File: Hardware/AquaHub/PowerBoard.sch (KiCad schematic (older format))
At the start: 22 parts, among them J1 Screw_Terminal_01x02, J11 Power_Conn, J2 Screw_Terminal_01x02, J3 Screw_Terminal_01x02, J4 Screw_Terminal_01x02, J5 Screw_Terminal_01x02, J6 Screw_Terminal_01x02, J7 Control_Conn, J8 Screw_Terminal_01x02, K1 5A Relay, K2 5A Relay, K3 5A Relay, K4 5A Relay, K5 5A Relay, K6 5A Relay, U2 Current Sense

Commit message: Commit latest hardware updates and initial firmware
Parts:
- C1: Farnell (none) -> CA07658; manf# GRM033R61C104ME14D -> (none)
- C2: Mouser (none) -> VJ0603A102GXAPW1BC; manf# VJ0603A102GXAPW1BC -> x
- J1, J2, J3, J4, J5, J6: Mouser (none) -> 1935161; manf# 1935161 -> x
- J7: renamed from J8; Mouser (none) -> 1935161; manf# 1935161 -> x
- K1, K2, K3, K4, K5, K6: Mouser (none) -> FTR-F1AA012V; manf# FTR-F1AA012V -> x
- R1: Mouser (none) -> GWCR0603-10KFT5; manf# GWCR0603-10KFT5 -> (none)
- RV1: Mouser (none) -> B72214P2251K101; manf# B72214P2251K101 -> x
- U2: Mouser (none) -> MLX91210KDC-CAS-102-SP; manf# MLX91210KDC-CAS-102-SP -> x
- V1: Mouser (none) -> RAC04-12SGB; manf# RAC04-12SGB -> (none)
- renumbered J7 to J8
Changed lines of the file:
@@
 P 3075 4200
 AR Path="/5BC6B929" Ref="J?"  Part="1"
-AR Path="/5B8F2634/5BC6B929" Ref="J7"  Part="1"
-F 0 "J7" H 3200 4175 50  0000 C CNN
+AR Path="/5B8F2634/5BC6B929" Ref="J8"  Part="1"
+F 0 "J8" H 3200 4175 50  0000 C CNN
 F 1 "Control_Conn" H 3150 4700 50  0000 C CNN
 F 2 "Connector_IDC:IDC-Header_2x05_P2.54mm_Vertical" H 3075 4200 50  0001 C CNN
@@
 F 2 "Relay_THT:Relay_DPST_Fujitsu_FTR-F1A" H 4650 5475 39  0001 C CNN
 F 3 "" H 4650 5475 39  0001 C CNN
-F 4 "FTR-F1AA012V" H 3450 5525 50  0001 C CNN "manf#"
-F 5 "Mouser" H -900 -450 50  0001 C CNN "Vendor"
+F 4 "Mouser" H -900 -450 50  0001 C CNN "Vendor"
+F 5 "FTR-F1AA012V" H 0   0   50  0001 C CNN "Mouser"
+F 6 "x" H 0   0   50  0001 C CNN "manf#"
 	1    3450 5525
 	1    0    0    -1
@@
 F 2 "Relay_THT:Relay_DPST_Fujitsu_FTR-F1A" H 6150 5475 39  0001 C CNN
 F 3 "" H 6150 5475 39  0001 C CNN
-F 4 "FTR-F1AA012V" H 3450 5525 50  0001 C CNN "manf#"
-F 5 "Mouser" H -900 -450 50  0001 C CNN "Vendor"
+F 4 "Mouser" H -900 -450 50  0001 C CNN "Vendor"
+F 5 "FTR-F1AA012V" H 0   0   50  0001 C CNN "Mouser"
+F 6 "x" H 0   0   50  0001 C CNN "manf#"
 	1    4950 5525
 	1    0    0    -1
@@
 F 2 "Relay_THT:Relay_DPST_Fujitsu_FTR-F1A" H 7650 5475 39  0001 C CNN
 F 3 "" H 7650 5475 39  0001 C CNN
-F 4 "FTR-F1AA012V" H 3450 5525 50  0001 C CNN "manf#"
-F 5 "Mouser" H -900 -450 50  0001 C CNN "Vendor"
+F 4 "Mouser" H -900 -450 50  0001 C CNN "Vendor"
+F 5 "FTR-F1AA012V" H 0   0   50  0001 C CNN "Mouser"
+F 6 "x" H 0   0   50  0001 C CNN "manf#"
 	1    6450 5525
 	1    0    0    -1
@@
 F 2 "Relay_THT:Relay_DPST_Fujitsu_FTR-F1A" H 9150 5475 39  0001 C CNN
 F 3 "" H 9150 5475 39  0001 C CNN
-F 4 "FTR-F1AA012V" H 3450 5525 50  0001 C CNN "manf#"
-F 5 "Mouser" H -900 -450 50  0001 C CNN "Vendor"
+F 4 "Mouser" H -900 -450 50  0001 C CNN "Vendor"
+F 5 "FTR-F1AA012V" H 0   0   50  0001 C CNN "Mouser"
+F 6 "x" H 0   0   50  0001 C CNN "manf#"
 	1    7950 5525
 	1    0    0    -1
@@
 F 2 "Relay_THT:Relay_DPST_Fujitsu_FTR-F1A" H 10650 5475 39  0001 C CNN
 F 3 "" H 10650 5475 39  0001 C CNN
-F 4 "FTR-F1AA012V" H 3450 5525 50  0001 C CNN "manf#"
-F 5 "Mouser" H -900 -450 50  0001 C CNN "Vendor"
+F 4 "Mouser" H -900 -450 50  0001 C CNN "Vendor"
+F 5 "FTR-F1AA012V" H 0   0   50  0001 C CNN "Mouser"
+F 6 "x" H 0   0   50  0001 C CNN "manf#"
 	1    9450 5525
 	1    0    0    -1
@@
 F 2 "Relay_THT:Relay_DPST_Fujitsu_FTR-F1A" H 3150 5475 39  0001 C CNN
 F 3 "" H 3150 5475 39  0001 C CNN
-F 4 "FTR-F1AA012V" H 1950 5525 50  0001 C CNN "manf#"
-F 5 "Mouser" H -900 -450 50  0001 C CNN "Vendor"
+F 4 "Mouser" H -900 -450 50  0001 C CNN "Vendor"
+F 5 "FTR-F1AA012V" H 0   0   50  0001 C CNN "Mouser"
+F 6 "x" H 0   0   50  0001 C CNN "manf#"
 	1    1950 5525
 	1    0    0    -1
@@
 F 2 "TerminalBlock_Phoenix:TerminalBlock_Phoenix_PT-1,5-2-5.0-H_1x02_P5.00mm_Horizontal" H 8200 4575 50  0001 C CNN
 F 3 "~" H 8200 4575 50  0001 C CNN
-F 4 "1935161" H 675 1250 50  0001 C CNN "manf#"
-F 5 "Mouser" H 325 1175 50  0001 C CNN "Vendor"
+F 4 "Mouser" H 325 1175 50  0001 C CNN "Vendor"
+F 5 "1935161" H 0   0   50  0001 C CNN "Mouser"
+F 6 "x" H 0   0   50  0001 C CNN "manf#"
 	1    8200 4575
 	-1   0    0    1
@@
 F 2 "TerminalBlock_Phoenix:TerminalBlock_Phoenix_PT-1,5-2-5.0-H_1x02_P5.00mm_Horizontal" H 8200 4350 50  0001 C CNN
 F 3 "~" H 8200 4350 50  0001 C CNN
-F 4 "1935161" H 675 1250 50  0001 C CNN "manf#"
-F 5 "Mouser" H 325 1175 50  0001 C CNN "Vendor"
+F 4 "Mouser" H 325 1175 50  0001 C CNN "Vendor"
+F 5 "1935161" H 0   0   50  0001 C CNN "Mouser"
+F 6 "x" H 0   0   50  0001 C CNN "manf#"
 	1    8200 4350
 	-1   0    0    1
@@
 F 2 "TerminalBlock_Phoenix:TerminalBlock_Phoenix_PT-1,5-2-5.0-H_1x02_P5.00mm_Horizontal" H 8200 4125 50  0001 C CNN
 F 3 "~" H 8200 4125 50  0001 C CNN
-F 4 "1935161" H 675 1250 50  0001 C CNN "manf#"
-F 5 "Mouser" H 325 1175 50  0001 C CNN "Vendor"
+F 4 "Mouser" H 325 1175 50  0001 C CNN "Vendor"
+F 5 "1935161" H 0   0   50  0001 C CNN "Mouser"
+F 6 "x" H 0   0   50  0001 C CNN "manf#"
 	1    8200 4125
 	-1   0    0    1
@@
 F 2 "TerminalBlock_Phoenix:TerminalBlock_Phoenix_PT-1,5-2-5.0-H_1x02_P5.00mm_Horizontal" H 8200 3900 50  0001 C CNN
 F 3 "~" H 8200 3900 50  0001 C CNN
-F 4 "1935161" H 675 1250 50  0001 C CNN "manf#"
-F 5 "Mouser" H 325 1175 50  0001 C CNN "Vendor"
+F 4 "Mouser" H 325 1175 50  0001 C CNN "Vendor"
+F 5 "1935161" H 0   0   50  0001 C CNN "Mouser"
+F 6 "x" H 0   0   50  0001 C CNN "manf#"
 	1    8200 3900
 	-1   0    0    1
@@
 F 2 "TerminalBlock_Phoenix:TerminalBlock_Phoenix_PT-1,5-2-5.0-H_1x02_P5.00mm_Horizontal" H 8200 3675 50  0001 C CNN
 F 3 "~" H 8200 3675 50  0001 C CNN
-F 4 "1935161" H 675 1250 50  0001 C CNN "manf#"
-F 5 "Mouser" H 325 1175 50  0001 C CNN "Vendor"
+F 4 "Mouser" H 325 1175 50  0001 C CNN "Vendor"
+F 5 "1935161" H 0   0   50  0001 C CNN "Mouser"
+F 6 "x" H 0   0   50  0001 C CNN "manf#"
 	1    8200 3675
 	-1   0    0    1
@@
 F 2 "TerminalBlock_Phoenix:TerminalBlock_Phoenix_PT-1,5-2-5.0-H_1x02_P5.00mm_Horizontal" H 8200 3450 50  0001 C CNN
 F 3 "~" H 8200 3450 50  0001 C CNN
-F 4 "1935161" H 675 1250 50  0001 C CNN "manf#"
-F 5 "Mouser" H 325 1175 50  0001 C CNN "Vendor"
+F 4 "Mouser" H 325 1175 50  0001 C CNN "Vendor"
+F 5 "1935161" H 0   0   50  0001 C CNN "Mouser"
+F 6 "x" H 0   0   50  0001 C CNN "manf#"
 	1    8200 3450
 	-1   0    0    1
@@
 P 4675 2675
 AR Path="/5BCFC420" Ref="J?"  Part="1"
-AR Path="/5B8F2634/5BCFC420" Ref="J8"  Part="1"
-F 0 "J8" H 4650 2475 50  0000 L CNN
+AR Path="/5B8F2634/5BCFC420" Ref="J7"  Part="1"
+F 0 "J7" H 4650 2475 50  0000 L CNN
 F 1 "Screw_Terminal_01x02" H 3875 2775 50  0001 L CNN
 F 2 "TerminalBlock_Phoenix:TerminalBlock_Phoenix_PT-1,5-2-5.0-H_1x02_P5.00mm_Horizontal" H 4675 2675 50  0001 C CNN
 F 3 "~" H 4675 2675 50  0001 C CNN
-F 4 "1935161" H 1500 -4450 50  0001 C CNN "manf#"
-F 5 "Mouser" H 1500 -4450 50  0001 C CNN "Vendor"
+F 4 "Mouser" H 1500 -4450 50  0001 C CNN "Vendor"
+F 5 "1935161" H 0   0   50  0001 C CNN "Mouser"
+F 6 "x" H 0   0   50  0001 C CNN "manf#"
 	1    4675 2675
 	-1   0    0    -1
@@
 F 2 "Package_SO:SOIC-8_3.9x4.9mm_P1.27mm" H 5500 3825 50  0001 L CIN
 F 3 "http://www.allegromicro.com/~/media/Files/Datasheets/ACS723-Datasheet.ashx?la=en" H 5400 4175 50  0001 C CNN
-F 4 "MLX91210KDC-CAS-102-SP" H -4050 1450 50  0001 C CNN "manf#"
-F 5 "Mouser" H -4100 1375 50  0001 C CNN "Vendor"
+F 4 "Mouser" H -4100 1375 50  0001 C CNN "Vendor"
+F 5 "MLX91210KDC-CAS-102-SP" H 0   0   50  0001 C CNN "Mouser"
+F 6 "x" H 0   0   50  0001 C CNN "manf#"
 	1    5400 4175
 	1    0    0    -1
@@
 F 2 "Capacitor_SMD:C_0603_1608Metric_Pad1.05x0.95mm_HandSolder" H 6013 4025 50  0001 C CNN
 F 3 "~" H 5975 4175 50  0001 C CNN
-F 4 "VJ0603A102GXAPW1BC" H -4175 1450 50  0001 C CNN "manf#"
-F 5 "Mouser" H -4100 1375 50  0001 C CNN "Vendor"
+F 4 "Mouser" H -4100 1375 50  0001 C CNN "Vendor"
+F 5 "VJ0603A102GXAPW1BC" H 0   0   50  0001 C CNN "Mouser"
+F 6 "x" H 0   0   50  0001 C CNN "manf#"
 	1    5975 4175
 	1    0    0    -1
@@
 F 2 "Capacitor_SMD:C_0603_1608Metric_Pad1.05x0.95mm_HandSolder" H 5688 3375 50  0001 C CNN
 F 3 "~" H 5650 3525 50  0001 C CNN
-F 4 "GRM033R61C104ME14D" H -4050 1450 50  0001 C CNN "manf#"
-F 5 "Mouser" H -4100 1375 50  0001 C CNN "Vendor"
+F 4 "Mouser" H -4100 1375 50  0001 C CNN "Vendor"
+F 5 "CA07658" H 0   0   50  0001 C CNN "Farnell"
 	1    5650 3525
 	0    1    1    0
@@
 F 2 "Resistor_SMD:R_0603_1608Metric_Pad1.05x0.95mm_HandSolder" V 6305 4200 50  0001 C CNN
 F 3 "~" H 6375 4200 50  0001 C CNN
-F 4 "GWCR0603-10KFT5" H -4175 1450 50  0001 C CNN "manf#"
-F 5 "Mouser" H -4100 1375 50  0001 C CNN "Vendor"
+F 4 "Mouser" H -4100 1375 50  0001 C CNN "Vendor"
+F 5 "GWCR0603-10KFT5" H 0   0   50  0001 C CNN "Mouser"
 	1    6375 4200
 	1    0    0    -1
@@
 F 2 "Converter_ACDC:Converter_ACDC_RECOM_RAC04-xxSGx_THT" H 3700 2800 50  0001 C CNN
 F 3 "" H 3700 2800 50  0001 C CNN
-F 4 "RAC04-12SGB" H 3850 2800 50  0001 C CNN "manf#"
+F 4 "RAC04-12SGB" H 0   0   50  0001 C CNN "Mouser"
 	1    3850 2800
 	1    0    0    -1
@@
 F 2 "Varistor:RV_Disc_D15.5mm_W6.1mm_P7.5mm" V 3180 2800 50  0001 C CNN
 F 3 "~" H 3250 2800 50  0001 C CNN
-F 4 "B72214P2251K101" H 3250 2800 50  0001 C CNN "manf#"
-F 5 "Mouser" H -5150 -1625 50  0001 C CNN "Vendor"
+F 4 "Mouser" H -5150 -1625 50  0001 C CNN "Vendor"
+F 5 "B72214P2251K101" H 0   0   50  0001 C CNN "Mouser"
+F 6 "x" H 0   0   50  0001 C CNN "manf#"
 	1    3250 2800
 	1    0    0    -1

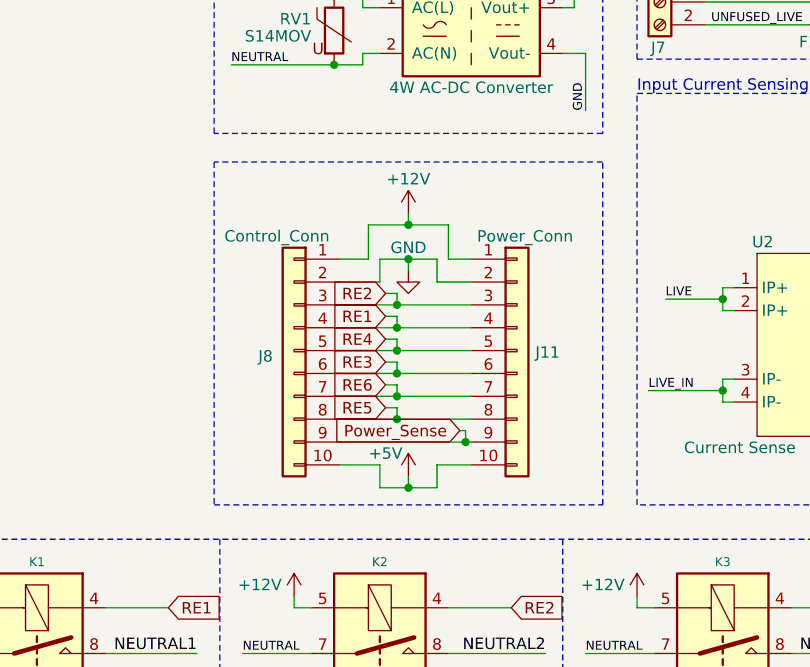
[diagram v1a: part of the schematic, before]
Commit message: Big PCB switch to a single board. Again.
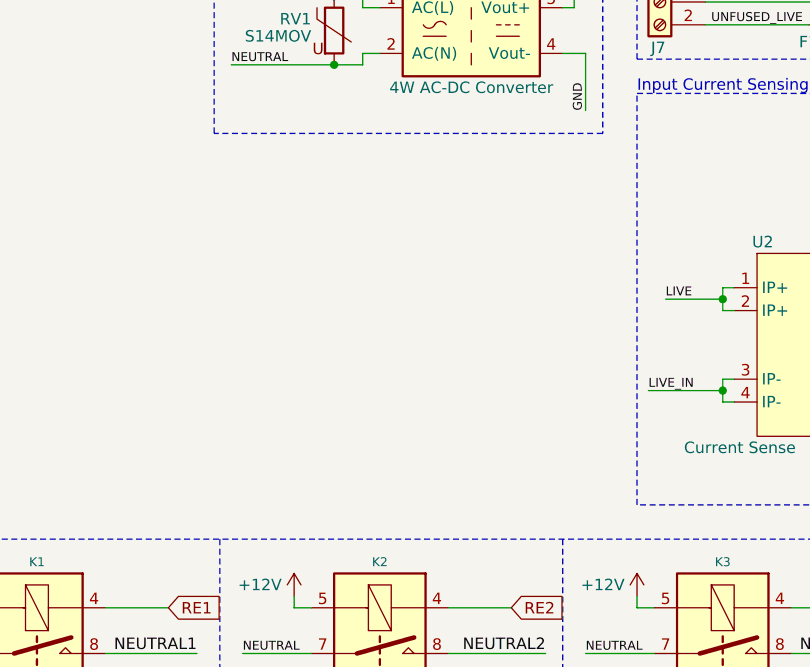
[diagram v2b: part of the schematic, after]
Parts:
- removed J11: Power_Conn, Connector_IDC:IDC-Header_2x05_P2.54mm_Vertical, symbol AquaHub-rescue:Conn_01x10-Connector_Generic
- removed J8: Control_Conn, Connector_IDC:IDC-Header_2x05_P2.54mm_Vertical, symbol AquaHub-rescue:Conn_01x10-Connector_Generic
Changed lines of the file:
@@
 Comment4 ""
 $EndDescr
-$Comp
-L AquaHub-rescue:Conn_01x10-Connector_Generic J?
-U 1 1 5BC6B922
-P 4050 4200
-AR Path="/5BC6B922" Ref="J?"  Part="1"
-AR Path="/5B8F2634/5BC6B922" Ref="J11"  Part="1"
-F 0 "J11" H 4130 4192 50  0000 L CNN
-F 1 "Power_Conn" H 3875 4700 50  0000 L CNN
-F 2 "Connector_IDC:IDC-Header_2x05_P2.54mm_Vertical" H 4050 4200 50  0001 C CNN
-F 3 "~" H 4050 4200 50  0001 C CNN
-F 4 "Mouser" H 1425 1750 50  0001 C CNN "Vendor"
-	1    4050 4200
-	1    0    0    -1
-$EndComp
-$Comp
-L AquaHub-rescue:Conn_01x10-Connector_Generic J?
-U 1 1 5BC6B929
-P 3075 4200
-AR Path="/5BC6B929" Ref="J?"  Part="1"
-AR Path="/5B8F2634/5BC6B929" Ref="J8"  Part="1"
-F 0 "J8" H 3200 4175 50  0000 C CNN
-F 1 "Control_Conn" H 3150 4700 50  0000 C CNN
-F 2 "Connector_IDC:IDC-Header_2x05_P2.54mm_Vertical" H 3075 4200 50  0001 C CNN
-F 3 "~" H 3075 4200 50  0001 C CNN
-	1    3075 4200
-	-1   0    0    -1
-$EndComp
-Wire Wire Line
-	3275 4000 3525 4000
-Wire Wire Line
-	3850 4100 3525 4100
-Wire Wire Line
-	3275 4200 3525 4200
-Wire Wire Line
-	3275 4300 3525 4300
-Wire Wire Line
-	3275 4400 3525 4400
-Wire Wire Line
-	3275 4500 3525 4500
-Wire Wire Line
-	3275 4600 3825 4600
-$Comp
-L AquaHub-rescue:+12V-power #PWR?
-U 1 1 5BC6B937
-P 3575 3600
-AR Path="/5BC6B937" Ref="#PWR?"  Part="1"
-AR Path="/5B8F2634/5BC6B937" Ref="#PWR0118"  Part="1"
-F 0 "#PWR0118" H 3575 3450 50  0001 C CNN
-F 1 "+12V" H 3575 3750 50  0000 C CNN
-F 2 "" H 3575 3600 50  0001 C CNN
-F 3 "" H 3575 3600 50  0001 C CNN
-	1    3575 3600
-	1    0    0    -1
-$EndComp
-Wire Wire Line
-	3575 3600 3575 3650
-$Comp
-L AquaHub-rescue:GND-power #PWR?
-U 1 1 5BC6B93E
-P 3575 3850
-AR Path="/5BC6B93E" Ref="#PWR?"  Part="1"
-AR Path="/5B8F2634/5BC6B93E" Ref="#PWR0119"  Part="1"
-F 0 "#PWR0119" H 3575 3600 50  0001 C CNN
-F 1 "GND" H 3575 3950 50  0000 C CNN
-F 2 "" H 3575 3850 50  0001 C CNN
-F 3 "" H 3575 3850 50  0001 C CNN
-	1    3575 3850
-	1    0    0    -1
-$EndComp
-Wire Wire Line
-	3275 3900 3450 3900
-Wire Wire Line
-	3450 3900 3450 3800
-Wire Wire Line
-	3450 3800 3575 3800
-Wire Wire Line
-	3575 3800 3575 3850
-Wire Wire Line
-	3575 3800 3700 3800
-Wire Wire Line
-	3700 3800 3700 3900
-Wire Wire Line
-	3700 3900 3850 3900
-Connection ~ 3575 3800
-Wire Wire Line
-	3275 3800 3400 3800
-Wire Wire Line
-	3400 3800 3400 3650
-Wire Wire Line
-	3400 3650 3575 3650
-Wire Wire Line
-	3750 3650 3750 3800
-Wire Wire Line
-	3750 3800 3850 3800
-Connection ~ 3575 3650
-Wire Wire Line
-	3575 3650 3750 3650
-$Comp
-L AquaHub-rescue:+5V-power #PWR?
-U 1 1 5BC6B95A
-P 3575 4750
-AR Path="/5BC6B95A" Ref="#PWR?"  Part="1"
-AR Path="/5B8F2634/5BC6B95A" Ref="#PWR0121"  Part="1"
-F 0 "#PWR0121" H 3575 4600 50  0001 C CNN
-F 1 "+5V" H 3475 4850 50  0000 C CNN
-F 2 "" H 3575 4750 50  0001 C CNN
-F 3 "" H 3575 4750 50  0001 C CNN
-	1    3575 4750
-	1    0    0    -1
-$EndComp
-Wire Wire Line
-	3275 4700 3450 4700
-Wire Wire Line
-	3450 4700 3450 4800
-Wire Wire Line
-	3450 4800 3575 4800
-Wire Wire Line
-	3700 4800 3700 4700
-Wire Wire Line
-	3700 4700 3850 4700
-Wire Wire Line
-	3575 4800 3575 4750
-Connection ~ 3575 4800
-Wire Wire Line
-	3575 4800 3700 4800
-Text GLabel 3475 4050 0    50   Input ~ 0
-RE1
-Wire Wire Line
-	3475 4050 3525 4050
-Wire Wire Line
-	3525 4050 3525 4100
-Connection ~ 3525 4100
-Wire Wire Line
-	3525 4100 3275 4100
-Text GLabel 3475 3950 0    50   Input ~ 0
-RE2
-Wire Wire Line
-	3475 3950 3525 3950
-Wire Wire Line
-	3525 3950 3525 4000
-Connection ~ 3525 4000
-Wire Wire Line
-	3525 4000 3850 4000
-Text GLabel 3475 4150 0    50   Input ~ 0
-RE4
-Text GLabel 3475 4250 0    50   Input ~ 0
-RE3
-Text GLabel 3475 4350 0    50   Input ~ 0
-RE6
-Text GLabel 3475 4450 0    50   Input ~ 0
-RE5
-Text GLabel 3800 4550 0    50   Input ~ 0
-Power_Sense
-Wire Wire Line
-	3800 4550 3825 4550
-Wire Wire Line
-	3825 4550 3825 4600
-Connection ~ 3825 4600
-Wire Wire Line
-	3825 4600 3850 4600
-Wire Wire Line
-	3475 4450 3525 4450
-Wire Wire Line
-	3525 4450 3525 4500
-Connection ~ 3525 4500
-Wire Wire Line
-	3525 4500 3850 4500
-Wire Wire Line
-	3475 4350 3525 4350
-Wire Wire Line
-	3525 4350 3525 4400
-Connection ~ 3525 4400
-Wire Wire Line
-	3525 4400 3850 4400
-Wire Wire Line
-	3475 4250 3525 4250
-Wire Wire Line
-	3525 4250 3525 4300
-Connection ~ 3525 4300
-Wire Wire Line
-	3525 4300 3850 4300
-Wire Wire Line
-	3475 4150 3525 4150
-Wire Wire Line
-	3525 4150 3525 4200
-Connection ~ 3525 4200
-Wire Wire Line
-	3525 4200 3850 4200
 Wire Notes Line style dotted
 	8750 5025 8750 6025
@@
 Text Label 1350 7600 2    39   ~ 0
 NEUTRAL
-Wire Notes Line
-	2725 3375 2725 4875
-Wire Notes Line
-	2725 4875 4425 4875
-Wire Notes Line
-	4425 4875 4425 3375
-Wire Notes Line
-	4425 3375 2725 3375
 $EndSCHEMATC
